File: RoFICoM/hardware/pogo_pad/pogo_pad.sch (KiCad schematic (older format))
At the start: 5 parts, among them J1 IN, J2 OUT, J3 POGO

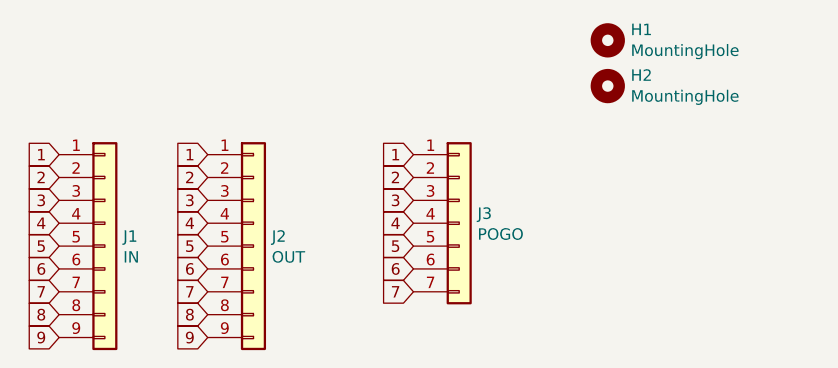
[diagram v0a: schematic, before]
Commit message: RoFICoM: Add Molex connector to pogo_pad
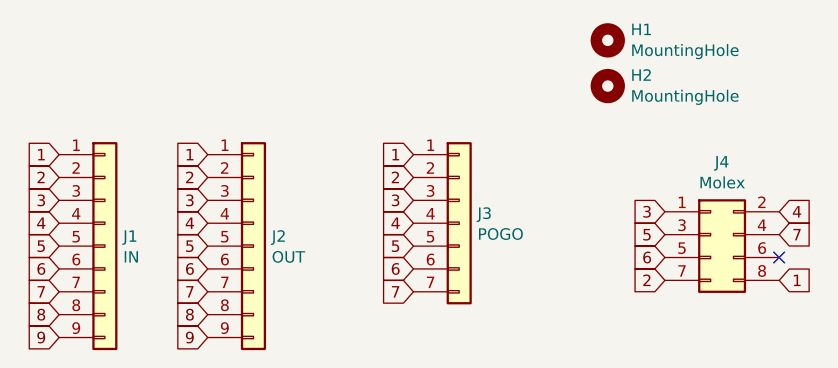
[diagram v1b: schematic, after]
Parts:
- added J4: Molex, rofi:molex-505004-0812, symbol Connector_Generic:Conn_02x04_Odd_Even
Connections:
- net 1: now also J4.8 (Pin_8)
- net 2: now also J4.7 (Pin_7)
- net 3: now also J4.1 (Pin_1)
- net 4: now also J4.2 (Pin_2)
- net 5: now also J4.3 (Pin_3)
- net 6: now also J4.5 (Pin_5)
- net 7: now also J4.4 (Pin_4)
- no-connect marks 0 -> 1
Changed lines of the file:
@@
 EESchema Schematic File Version 4
-EELAYER 26 0
+LIBS:pogo_pad-cache
+EELAYER 29 0
 EELAYER END
 $Descr A4 11693 8268
@@
 Text GLabel 3950 3950 0    50   Input ~ 0
 9
+Text GLabel 6600 3400 0    50   Input ~ 0
+3
+Text GLabel 7100 3400 2    50   Input ~ 0
+4
+Text GLabel 6600 3500 0    50   Input ~ 0
+5
+Text GLabel 7100 3500 2    50   Input ~ 0
+7
+Text GLabel 6600 3600 0    50   Input ~ 0
+6
+NoConn ~ 7100 3600
+Text GLabel 6600 3700 0    50   Input ~ 0
+2
+Text GLabel 7100 3700 2    50   Input ~ 0
+1
+$Comp
+L Connector_Generic:Conn_02x04_Odd_Even J4
+U 1 1 5D6FDCDA
+P 6800 3500
+F 0 "J4" H 6850 3817 50  0000 C CNN
+F 1 "Molex" H 6850 3726 50  0000 C CNN
+F 2 "rofi:molex-505004-0812" H 6800 3500 50  0001 C CNN
+F 3 "~" H 6800 3500 50  0001 C CNN
+	1    6800 3500
+	1    0    0    -1
+$EndComp
 $EndSCHEMATC
